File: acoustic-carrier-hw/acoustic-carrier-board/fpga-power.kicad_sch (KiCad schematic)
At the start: 87 parts, among them IC1 ECP5-BGA256, J3 Conn_02x08_Odd_Even, Q1 AO3401A, U10 TLV62569DBV, U11 TLV62569DBV, U14 TLV62569DBV, U16 TPS2121RUX, U5 OPA376xxDBV, U8 TLV62569DBV

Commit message: [carrier] Added hierarchical labels
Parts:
- removed C11, C12, C13, C14, C26, C31, C41, C74, C75: 10uF, Capacitor_SMD:C_0603_1608Metric, symbol Device:C_Small
- removed C15: 47uF, Capacitor_SMD:C_0805_2012Metric, symbol Device:C_Small
- removed C16, C33, C36, C45, C48, C50, C51, C52, C61, C62, C63, C64, C65, C66: 0.1uF, Capacitor_SMD:C_0402_1005Metric, symbol Device:C_Small
- removed C17: 150uF, Capacitor_SMD:CP_Elec_8x6.2, symbol Device:C_Polarized_Small
- removed C18, C19, C20, C21: 10pF, Capacitor_SMD:C_0402_1005Metric, symbol Device:C_Small
- removed C27, C28, C29, C69, C76: 4.7uF, Capacitor_SMD:C_0402_1005Metric, symbol Device:C_Small
- removed C53, C60: 470nF, Capacitor_SMD:C_0603_1608Metric, symbol Device:C_Small
- removed C54, C55, C56, C68: 1uF, Capacitor_SMD:C_0805_2012Metric, symbol Device:C_Small
- removed J3: Conn_02x08_Odd_Even, Connector_PinSocket_2.54mm:PinSocket_2x08_P2.54mm_Horizontal, symbol Connector_Generic:Conn_02x08_Odd_Even
- removed L2, L3, L7: 2.2uH, iw-inductor:L_Changjiang_FNR4018S, symbol Device:L_Small
- removed Q1: AO3401A, Package_TO_SOT_SMD:SOT-23, symbol Transistor_FET:AO3401A
- removed R100: 220, Resistor_SMD:R_0603_1608Metric, symbol Device:R_Small
- removed R11: 100k, Resistor_SMD:R_0603_1608Metric_Pad0.98x0.95mm_HandSolder, symbol Device:R_Small
- removed R12: 27k, Resistor_SMD:R_0603_1608Metric, symbol Device:R_Small
- removed R13, R16: 5.1k, Resistor_SMD:R_0603_1608Metric, symbol Device:R_Small
- removed R14, R15: 24k, Resistor_SMD:R_0603_1608Metric, symbol Device:R_Small
- removed R17: 22k, Resistor_SMD:R_0603_1608Metric, symbol Device:R_Small
- removed R3, R6, R7, R8: 0, Resistor_SMD:R_0805_2012Metric_Pad1.20x1.40mm_HandSolder, symbol Device:R_Small
- removed R4, R5, R56: 1k, Resistor_SMD:R_0603_1608Metric, symbol Device:R_Small
- removed R59, R63: 24k, Resistor_SMD:R_0603_1608Metric, symbol Device:R
- removed R60, R99: 0, Resistor_SMD:R_0603_1608Metric, symbol Device:R_Small
- removed R61, R64, R65: 100k, Resistor_SMD:R_0402_1005Metric, symbol Device:R
- removed R62: 22k, Resistor_SMD:R_0603_1608Metric, symbol Device:R
- removed R97: 75k, Resistor_SMD:R_0603_1608Metric, symbol Device:R
- removed R98: 30k, Resistor_SMD:R_0603_1608Metric, symbol Device:R
- removed TP4, TP5, TP6, TP7: TestPoint_Small, TestPoint:TestPoint_Pad_D1.5mm, symbol Connector:TestPoint_Small
- removed TP9: TestPoint, TestPoint:TestPoint_Pad_1.0x1.0mm, symbol Connector:TestPoint
- removed U10, U11, U14, U8: TLV62569DBV, Package_TO_SOT_SMD:SOT-23-5, symbol Regulator_Switching:TLV62569DBV
- removed U16: TPS2121RUX, iw-power:TPS2121, symbol iw-power:TPS2121RUXR
- removed U5: OPA376xxDBV, Package_TO_SOT_SMD:SOT-23-5, symbol Amplifier_Operational:OPA376xxDBV
- added C146, C149, C150, C151, C152, C172, C173: 0.1uF, Capacitor_SMD:C_0402_1005Metric, symbol Device:C_Small
- added C153: 10uF, Capacitor_SMD:C_0603_1608Metric, symbol Device:C_Small
- C10: value 10uF -> 4.7uF; footprint Capacitor_SMD:C_0603_1608Metric -> Capacitor_SMD:C_0402_1005Metric; LPN C19702 -> C23733; MPN CL10A106KP8NNNC -> CL05A475MP5NRNC
- C7: value 10uF -> 0.1uF; footprint Capacitor_SMD:C_0603_1608Metric -> Capacitor_SMD:C_0402_1005Metric; LPN C19702 -> C307331; MPN CL10A106KP8NNNC -> CL05B104KB54PNC
- C9: value 10uF -> 22uF; LPN C19702 -> C59461; MPN CL10A106KP8NNNC -> CL10A226MQ8NRNC
- L1: value 2.2uH -> 120@100MHz; footprint iw-inductor:L_Changjiang_FNR4018S -> Inductor_SMD:L_0603_1608Metric; LPN C28642347 -> C113030; MPN NR4018S2R2MT -> BLM18SG121TN1D
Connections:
- net +1V2 is gone; now on net VCORE_3V3: C7.1
- net +2V5 is gone; now on an unnamed net: C10.1, C9.1
- net GND: now also C146.2, C149.2, C150.2, C151.2, C152.2, C153.2, C172.2, C173.2
- net VAUX_2V5: now also L1.2; no longer IC1.G11 (VCCAUX_1), IC1.L7 (VCCAUX_2)
- net VCORE_3V3: now also C8.1, C146.1, C149.1, C150.1, C151.1, C152.1, C153.1
- net at L1.1: now also IC1.G11 (VCCAUX_1), IC1.L7 (VCCAUX_2), C172.1, C173.1
- removed net +1V35: C8.1, L1.2
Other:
- note added: "RECOMMENDED: - min 100 nF per pin - 1 uF for extra decoupling - Extra 22 uF due to ferrite"
- note added: "RECOMMENDED: - min 100 nF per pin - 10 uF per 5 pins"
- note removed: "AUXILIARY SUPPLY"
- note removed: "Bank 2, 6 PIO supply voltage (DDR3L)"
- note removed: "CORE SUPPLY"
- note removed: "Ethernet Supply Voltage"
- note removed: "PIO DECOUPLING"
- note removed: "Power Board (power connector)"
- note removed: "R2 value: - Make sure the R2's are all < 200 kOhm (datasheet recommendations) Capacitor - f_zero = 1/(2*pi*R2*10e-12) = 159 kHz for 100 kOhm, 10 pF - Response time for fb loop decreases by 50 % compared to 6.8 pF case R2/R1 ratio: - 0.6 * (1+R1/R2) = Vout"
- note removed: "REVERSE VOLTAGE PROTECTION MOSFET - Imax: 5.7 A - Vgs_max 12 V - Rdson: 85m-50m ANODE / CATHODE source drain connection - Switched around, becuase normally input: voltage regulator - Main thing: Vgs high enough -> pushed high anyways"
- note removed: "R_ILM: - 27 kOhm, current limiting [4 amps] SS: - Settling time, time to wait for the switch to open once input voltage is valid - 0.1 uF: 780 V / s -> 6.4 ms OP1/2: - Voltage reference (1.01 .. 1.1) - When OP1/2 input > reference => turned off / channel switch - Choose 5.1, 22 kOhm VDIV -> 1.05 / [5.1 / (24+5.1)] = 6 V PR: - Connect to GND (not req) CP2: - Enables comparator operation (external 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"
- note removed: "Test Point 2v5"
- note removed: "Test Point 3v3"
- note removed: "Vref - Ability to chose between R-div and OPAMP OPA376 - Precision amplifier, buffers Vref - Resistor in front to avoid instabilities (capacitive load) - Current sourcing / sinking > 1 mA - 0.675 / 225 ohm = 3 mA -> limit current"
- moved on the sheet: IC1A

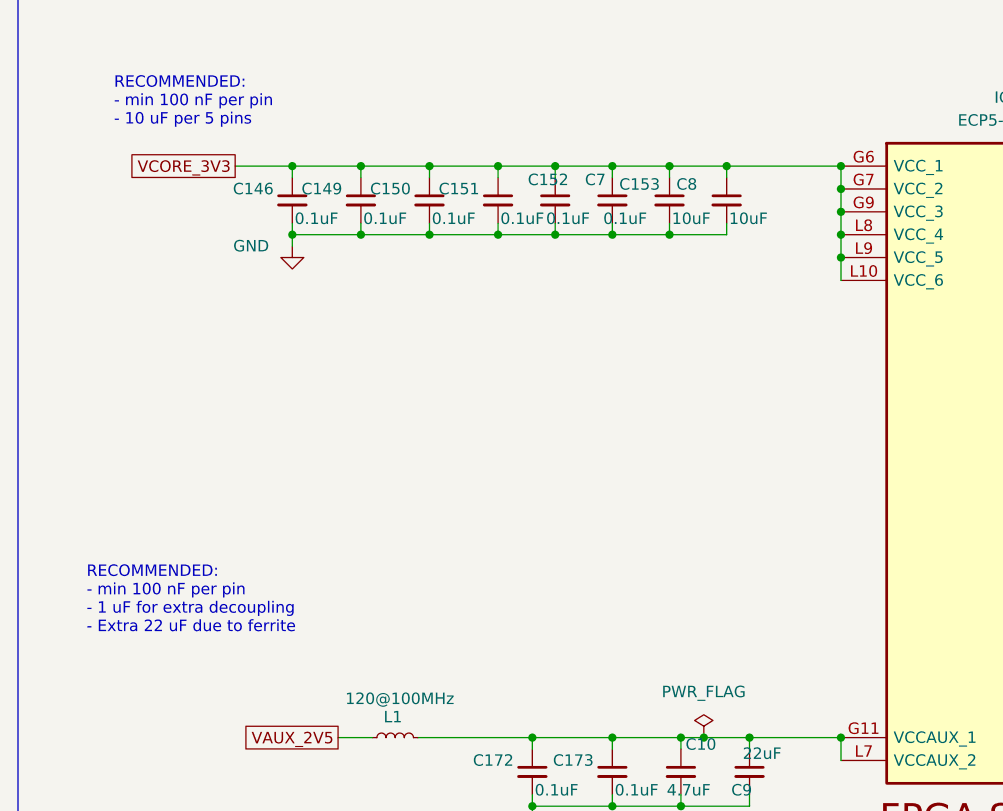
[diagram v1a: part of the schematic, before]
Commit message: [carrier] Added extra decoupling to ECP5U according to datasheet (next) perform page-wise checks, add testpoints
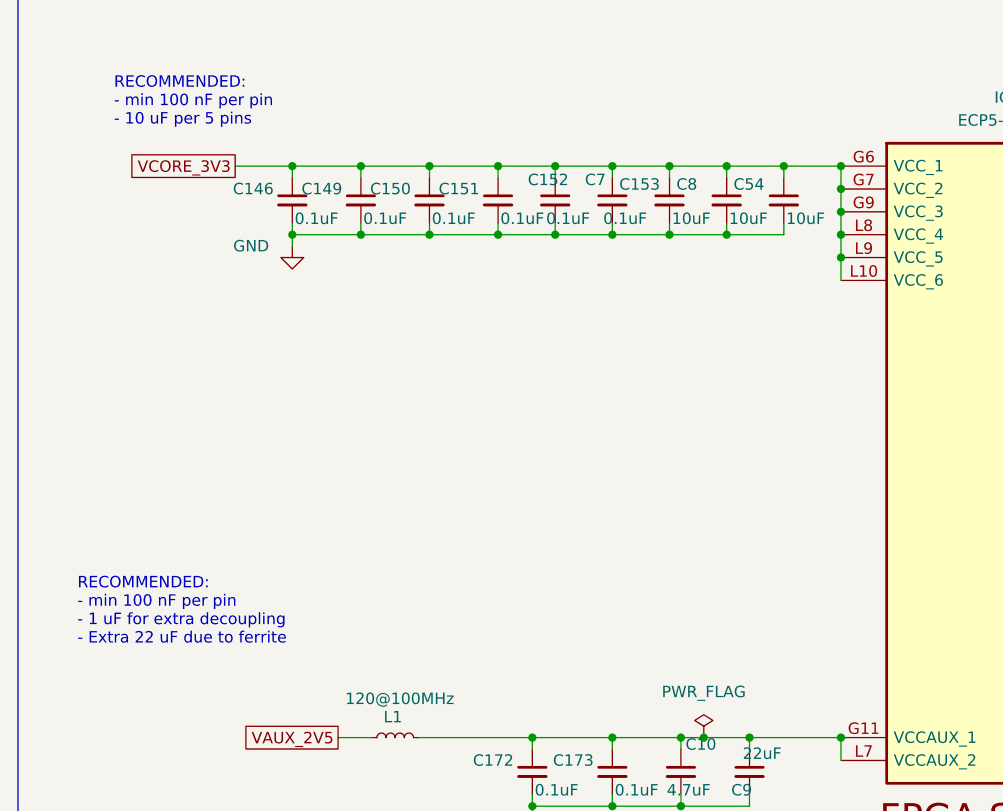
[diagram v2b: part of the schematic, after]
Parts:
- added C54: 10uF, Capacitor_SMD:C_0603_1608Metric, symbol Device:C_Small
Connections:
- net GND: now also C54.2
- net VCORE_3V3: now also C54.1
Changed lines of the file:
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@@
 	(text "RECOMMENDED:\n- min 100 nF per pin\n- 1 uF for extra decoupling\n- Extra 22 uF due to ferrite"
 		(exclude_from_sim no)
-		(at 92.71 109.22 0)
+		(at 91.694 110.49 0)
 		(effects
 			(font
@@
 	)
 	(junction
+		(at 170.18 60.96)
+		(diameter 0)
+		(color 0 0 0 0)
+	)
+	(junction
+		(at 163.83 68.58)
+		(diameter 0)
+		(color 0 0 0 0)
+	)
+	(junction
 		(at 138.43 60.96)
 		(diameter 0)
@@
 	(wire
 		(pts
-			(xy 163.83 68.58) (xy 157.48 68.58)
+			(xy 157.48 68.58) (xy 163.83 68.58)
 		)
 		(stroke
@@
 	(wire
 		(pts
+			(xy 170.18 60.96) (xy 176.53 60.96)
+		)
+		(stroke
+			(width 0)
+			(type default)
+		)
+	)
+	(wire
+		(pts
 			(xy 214.63 88.9) (xy 214.63 91.44)
 		)
@@
 	(wire
 		(pts
-			(xy 163.83 60.96) (xy 176.53 60.96)
+			(xy 163.83 60.96) (xy 170.18 60.96)
 		)
 		(stroke
@@
 	(wire
 		(pts
+			(xy 170.18 60.96) (xy 170.18 62.23)
+		)
+		(stroke
+			(width 0)
+			(type default)
+		)
+	)
+	(wire
+		(pts
 			(xy 158.75 125.73) (xy 158.75 124.46)
 		)
@@
 	(wire
 		(pts
+			(xy 170.18 67.31) (xy 170.18 68.58)
+		)
+		(stroke
+			(width 0)
+			(type default)
+		)
+	)
+	(wire
+		(pts
 			(xy 129.54 124.46) (xy 142.24 124.46)
 		)
@@
 	(wire
 		(pts
+			(xy 163.83 68.58) (xy 170.18 68.58)
+		)
+		(stroke
+			(width 0)
+			(type default)
+		)
+	)
+	(wire
+		(pts
 			(xy 158.75 132.08) (xy 166.37 132.08)
 		)
@@
 					(unit 1)
 				)
+			)
+		)
+	)
+	(symbol
+		(lib_id "Device:C_Small")
+		(at 170.18 64.77 0)
+		(unit 1)
+		(exclude_from_sim no)
+		(in_bom yes)
+		(on_board yes)
+		(dnp no)
+		(property "Reference" "C54"
+			(at 164.592 62.992 0)
+			(effects
+				(font
+					(size 1.27 1.27)
+				)
+				(justify left)
+			)
+		)
+		(property "Value" "10uF"
+			(at 170.434 66.802 0)
+			(effects
+				(font
+					(size 1.27 1.27)
+				)
+				(justify left)
+			)
+		)
+		(property "Footprint" "Capacitor_SMD:C_0603_1608Metric"
+			(at 170.18 64.77 0)
+			(effects
+				(font
+					(size 1.27 1.27)
+				)
+				(hide yes)
+			)
+		)
+		(property "Datasheet" "~"
+			(at 170.18 64.77 0)
+			(effects
+				(font
+					(size 1.27 1.27)
+				)
+				(hide yes)
+			)
+		)
+		(property "Description" "X5R, 10V"
+			(at 170.18 64.77 0)
+			(effects
+				(font
+					(size 1.27 1.27)
+				)
+				(hide yes)
+			)
+		)
+		(property "LPN" "C19702"
+			(at 170.18 64.77 0)
+			(effects
+				(font
+					(size 1.27 1.27)
+				)
+				(hide yes)
+			)
+		)
+		(property "MPN" "CL10A106KP8NNNC"
+			(at 170.18 64.77 0)
+			(effects
+				(font
+					(size 1.27 1.27)
+				)
+				(hide yes)
+			)
+		)
+		(property "Part Number" ""
+			(at 170.18 64.77 0)
+			(effects
+				(font
+					(size 1.27 1.27)
+				)
+				(hide yes)
+			)
+		)
+		(property "SN-DK" ""
+			(at 170.18 64.77 0)
+			(effects
+				(font
+					(size 1.27 1.27)
+				)
+				(hide yes)
+			)
+		)
+		(property "Sim.Pin" ""
+			(at 170.18 64.77 0)
+			(effects
+				(font
+					(size 1.27 1.27)
+				)
+				(hide yes)
+			)
+		)
+		(property "LCSC Part" ""
+			(at 170.18 64.77 0)
+			(effects
+				(font
+					(size 1.27 1.27)
+				)
+				(hide yes)
+			)
+		)
+		(pin "2"
+		)
+		(pin "1"
+		)
+		(instances
+			(project "acoustic-carrier-board"
+				(path "/25b015c9-ab13-4427-b72c-b6f348597100/aad6bec2-3cac-4ef0-abf0-8e1f80301155"
+					(reference "C54")
+					(unit 1)
+				)

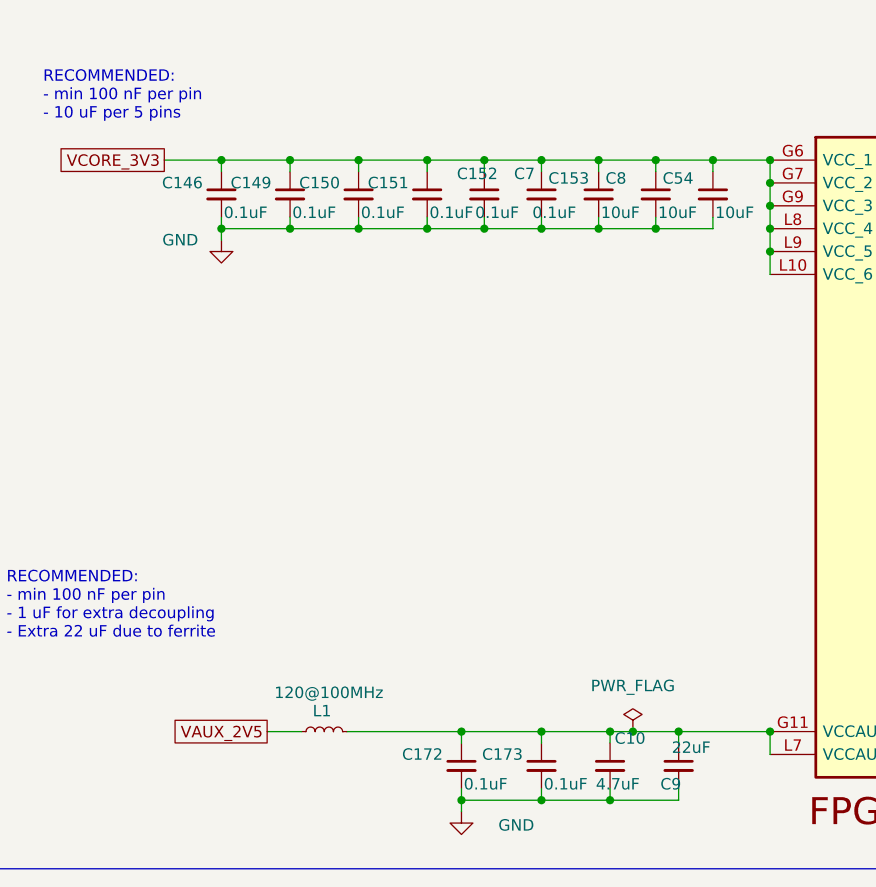
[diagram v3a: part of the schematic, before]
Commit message: [carrier] Finished rough layout, p (put together according to component category
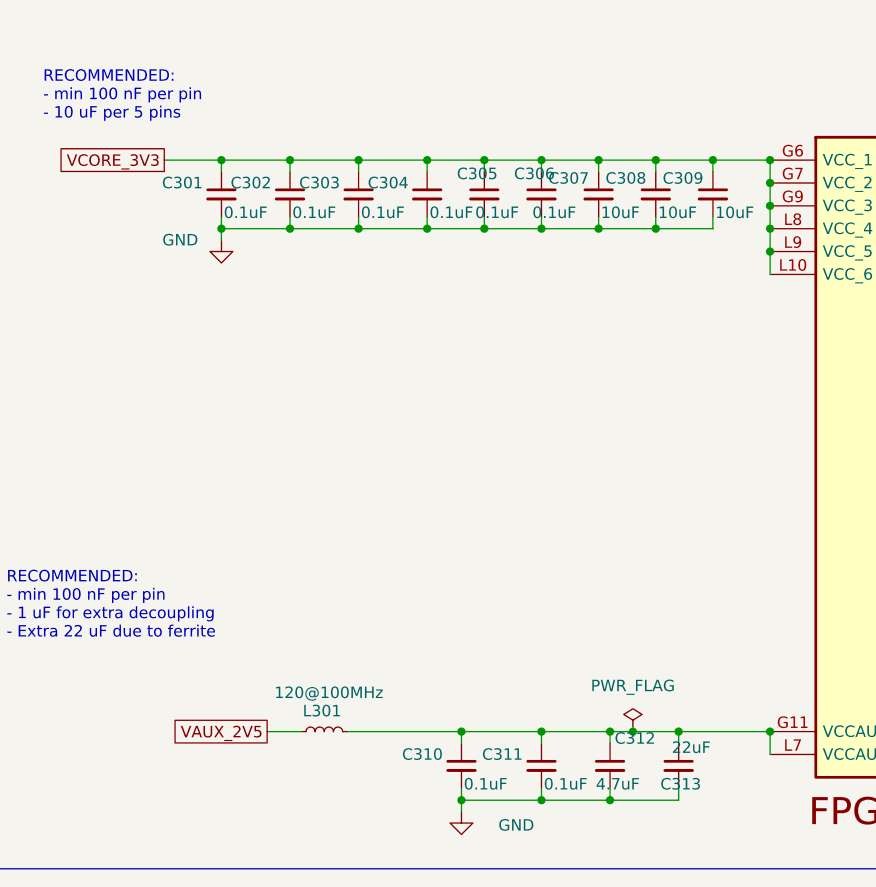
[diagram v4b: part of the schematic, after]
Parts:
- renumbered C146 to C301, C149 to C302, C150 to C303, C151 to C304, C152 to C305, C7 to C306, C153 to C307, C8 to C308, C54 to C309, C172 to C310, C173 to C311, C10 to C312, C9 to C313, L1 to L301
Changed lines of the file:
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@@
 		(on_board yes)
 		(dnp no)
-		(property "Reference" "C10"
+		(property "Reference" "C312"
 			(at 159.258 125.222 0)
 			(effects
@@
 			(project "acoustic-carrier-board"
 				(path "/25b015c9-ab13-4427-b72c-b6f348597100/aad6bec2-3cac-4ef0-abf0-8e1f80301155"
-					(reference "C10")
+					(reference "C312")
 					(unit 1)
 				)
@@
 		(on_board yes)
 		(dnp no)
-		(property "Reference" "C152"
+		(property "Reference" "C305"
 			(at 141.732 62.484 0)
 			(effects
@@
 			(project "acoustic-carrier-board"
 				(path "/25b015c9-ab13-4427-b72c-b6f348597100/aad6bec2-3cac-4ef0-abf0-8e1f80301155"
-					(reference "C152")
+					(reference "C305")
 					(unit 1)
 				)
@@
 		(on_board yes)
 		(dnp no)
-		(property "Reference" "#PWR0117"
+		(property "Reference" "#PWR0301"
 			(at 115.57 76.2 0)
 			(effects
@@
 			(project "acoustic-carrier-board"
 				(path "/25b015c9-ab13-4427-b72c-b6f348597100/aad6bec2-3cac-4ef0-abf0-8e1f80301155"
-					(reference "#PWR0117")
+					(reference "#PWR0301")
 					(unit 1)
 				)
@@
 		(dnp no)
 		(fields_autoplaced yes)
-		(property "Reference" "#PWR016"
+		(property "Reference" "#PWR0302"
 			(at 214.63 134.62 0)
 			(effects
@@
 			(project "acoustic-carrier-board"
 				(path "/25b015c9-ab13-4427-b72c-b6f348597100/aad6bec2-3cac-4ef0-abf0-8e1f80301155"
-					(reference "#PWR016")
+					(reference "#PWR0302")
 					(unit 1)
 				)
@@
 		(on_board yes)
 		(dnp no)
-		(property "Reference" "C153"
+		(property "Reference" "C307"
 			(at 151.892 62.992 0)
 			(effects
@@
 			(project "acoustic-carrier-board"
 				(path "/25b015c9-ab13-4427-b72c-b6f348597100/aad6bec2-3cac-4ef0-abf0-8e1f80301155"
-					(reference "C153")
+					(reference "C307")
 					(unit 1)
 				)
@@
 		(on_board yes)
 		(dnp no)
-		(property "Reference" "#PWR0168"
+		(property "Reference" "#PWR0303"
 			(at 142.24 139.7 0)
 			(effects
@@
 			(project "acoustic-carrier-board"
 				(path "/25b015c9-ab13-4427-b72c-b6f348597100/aad6bec2-3cac-4ef0-abf0-8e1f80301155"
-					(reference "#PWR0168")
+					(reference "#PWR0303")
 					(unit 1)
 				)
@@
 		(on_board yes)
 		(dnp no)
-		(property "Reference" "L1"
+		(property "Reference" "L301"
 			(at 126.746 122.174 90)
 			(effects
@@
 			(project "acoustic-carrier-board"
 				(path "/25b015c9-ab13-4427-b72c-b6f348597100/aad6bec2-3cac-4ef0-abf0-8e1f80301155"
-					(reference "L1")
+					(reference "L301")
 					(unit 1)
 				)
@@
 		(on_board yes)
 		(dnp no)
-		(property "Reference" "C173"
+		(property "Reference" "C311"
 			(at 144.526 127 0)
 			(effects
@@
 			(project "acoustic-carrier-board"
 				(path "/25b015c9-ab13-4427-b72c-b6f348597100/aad6bec2-3cac-4ef0-abf0-8e1f80301155"
-					(reference "C173")
+					(reference "C311")
 					(unit 1)
 				)
@@
 		(on_board yes)
 		(dnp no)
-		(property "Reference" "C8"
+		(property "Reference" "C308"
 			(at 158.242 62.992 0)
 			(effects
@@
 			(project "acoustic-carrier-board"
 				(path "/25b015c9-ab13-4427-b72c-b6f348597100/aad6bec2-3cac-4ef0-abf0-8e1f80301155"
-					(reference "C8")
+					(reference "C308")
 					(unit 1)
 				)
@@
 		(on_board yes)
 		(dnp no)
-		(property "Reference" "C149"
+		(property "Reference" "C302"
 			(at 116.586 63.5 0)
 			(effects
@@
 			(project "acoustic-carrier-board"
 				(path "/25b015c9-ab13-4427-b72c-b6f348597100/aad6bec2-3cac-4ef0-abf0-8e1f80301155"
-					(reference "C149")
+					(reference "C302")
 					(unit 1)
 				)
@@
 		(on_board yes)
 		(dnp no)
-		(property "Reference" "C9"
+		(property "Reference" "C313"
 			(at 164.338 130.302 0)
 			(effects
@@
 			(project "acoustic-carrier-board"
 				(path "/25b015c9-ab13-4427-b72c-b6f348597100/aad6bec2-3cac-4ef0-abf0-8e1f80301155"
-					(reference "C9")
+					(reference "C313")
 					(unit 1)
 				)
@@
 		(on_board yes)
 		(dnp no)
-		(property "Reference" "C7"
+		(property "Reference" "C306"
 			(at 148.082 62.484 0)
 			(effects
@@
 			(project "acoustic-carrier-board"
 				(path "/25b015c9-ab13-4427-b72c-b6f348597100/aad6bec2-3cac-4ef0-abf0-8e1f80301155"
-					(reference "C7")
+					(reference "C306")
 					(unit 1)
 				)
@@
 		(on_board yes)
 		(dnp no)
-		(property "Reference" "C151"
+		(property "Reference" "C304"
 			(at 131.826 63.5 0)
 			(effects
@@
 			(project "acoustic-carrier-board"
 				(path "/25b015c9-ab13-4427-b72c-b6f348597100/aad6bec2-3cac-4ef0-abf0-8e1f80301155"
-					(reference "C151")
+					(reference "C304")
 					(unit 1)
 				)
@@
 		(on_board yes)
 		(dnp no)
-		(property "Reference" "C146"
+		(property "Reference" "C301"
 			(at 108.966 63.5 0)
 			(effects
@@
 			(project "acoustic-carrier-board"
 				(path "/25b015c9-ab13-4427-b72c-b6f348597100/aad6bec2-3cac-4ef0-abf0-8e1f80301155"
-					(reference "C146")
+					(reference "C301")
 					(unit 1)
 				)
@@
 		(on_board yes)
 		(dnp no)
-		(property "Reference" "C150"
+		(property "Reference" "C303"
 			(at 124.206 63.5 0)
 			(effects
@@
 			(project "acoustic-carrier-board"
 				(path "/25b015c9-ab13-4427-b72c-b6f348597100/aad6bec2-3cac-4ef0-abf0-8e1f80301155"
-					(reference "C150")
+					(reference "C303")
 					(unit 1)
 				)
@@
 		(dnp no)
 		(fields_autoplaced yes)
-		(property "Reference" "#FLG04"
+		(property "Reference" "#FLG0301"
 			(at 161.29 122.555 0)
 			(effects
@@
 			(project ""
 				(path "/25b015c9-ab13-4427-b72c-b6f348597100/aad6bec2-3cac-4ef0-abf0-8e1f80301155"
-					(reference "#FLG04")
+					(reference "#FLG0301")
 					(unit 1)
 				)
@@
 		(on_board yes)
 		(dnp no)
-		(property "Reference" "C54"
+		(property "Reference" "C309"
 			(at 164.592 62.992 0)
 			(effects
@@
 			(project "acoustic-carrier-board"
 				(path "/25b015c9-ab13-4427-b72c-b6f348597100/aad6bec2-3cac-4ef0-abf0-8e1f80301155"
-					(reference "C54")
+					(reference "C309")
 					(unit 1)
 				)
@@
 		(on_board yes)
 		(dnp no)
-		(property "Reference" "C172"
+		(property "Reference" "C310"
 			(at 135.636 127 0)
 			(effects
@@
 			(project "acoustic-carrier-board"
 				(path "/25b015c9-ab13-4427-b72c-b6f348597100/aad6bec2-3cac-4ef0-abf0-8e1f80301155"
-					(reference "C172")
+					(reference "C310")
 					(unit 1)
 				)
